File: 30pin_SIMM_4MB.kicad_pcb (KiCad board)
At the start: 2 copper layers, 88.9 x 20 mm, 7 parts, among them IC1 4Mx4bit_DRAM, IC2 4Mx4bit_DRAM, IC3 4Mx1bit_DRAM, J1 30pin_SIMM_Edge

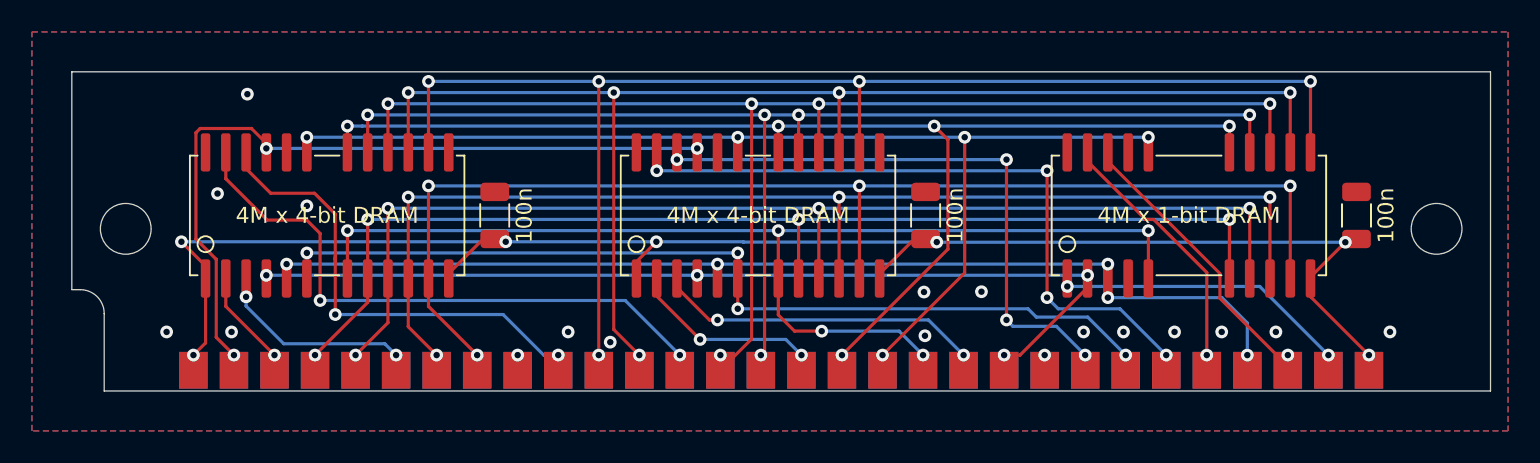
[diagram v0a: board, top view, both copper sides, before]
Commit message: Added silkscreen
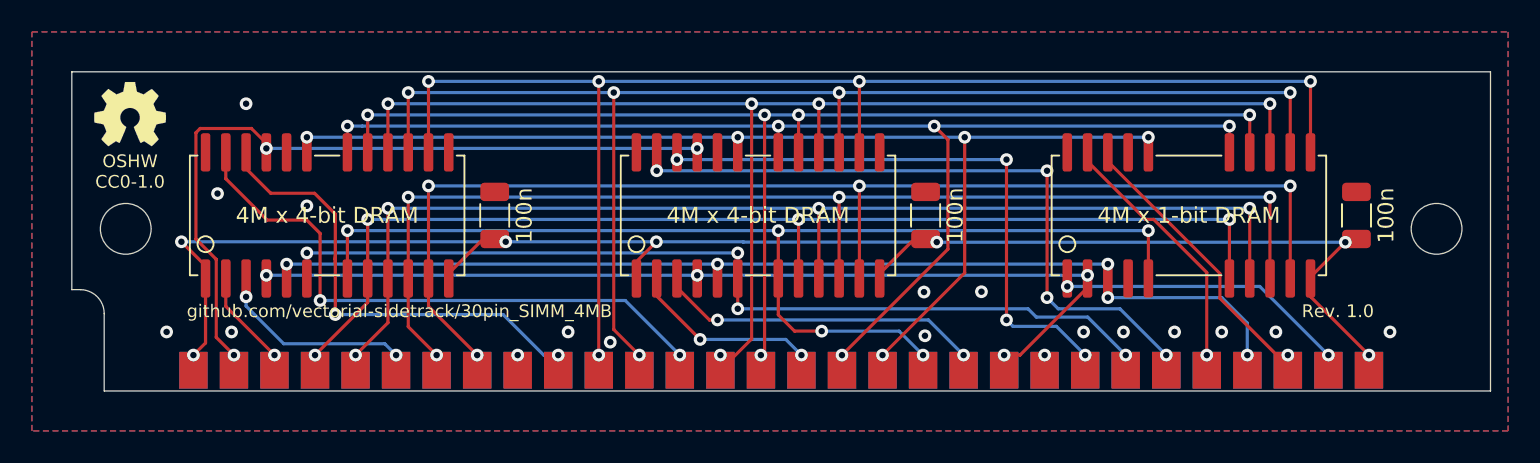
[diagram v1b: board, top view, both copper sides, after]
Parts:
- added REF**: OSHW-Symbol_5.7x6mm_SilkScreen, 30pin_SIMM:OSHW-Symbol_5.7x6mm_SilkScreen, F.Cu at (103.7, 82.8)
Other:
- board text added: "30 pin SIMM 4 MB + Parity"
- board text added: "OSHW CC0-1.0"
- board text added: "Rev. 1.0"
- board text added: "github.com/vectorial-sidetrack/30pin_SIMM_4MB"
- board text added: "ns"

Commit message: Added mounting holes as footprints and NPTH
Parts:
- added REF**: MountingHole_3.18mm, 30pin_SIMM:MountingHole_3.18mm, F.Cu at (103.4, 89.8)
- added REF**: MountingHole_3.18mm, 30pin_SIMM:MountingHole_3.18mm, F.Cu at (185.5, 89.8)
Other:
- outline, holes or cut-outs redrawn
- board text added: "JLCJLCJLCJLC"
